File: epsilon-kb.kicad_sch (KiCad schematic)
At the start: 36 parts, among them J1 OLED-128x64, J2 OLED-128x32, J3 Conn_01x01, SW1 SW_Push, SW10 SW_Push, SW11 SW_SPDT, SW2 SW_Push, SW3 SW_Push, SW4 SW_Push, SW5 SW_Push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

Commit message: PCB
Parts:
- removed J3: Conn_01x01, symbol Connector_Generic:Conn_01x01
- added SW12: SW_Push, Button_Switch_THT:SW_PUSH_6mm, symbol Switch:SW_Push
- D1, D10, D2, D3, D4, D5, D6, D7, D8, D9: value SK6812MINI -> SK6812MINI-E; symbol LED:SK6812MINI -> sk6812mini-e:SK6812MINI-E
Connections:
- net +5V: now also D1.1 (VDD), D10.1 (VDD), D2.1 (VDD), D3.1 (VDD), D4.1 (VDD), D5.1 (VDD), D6.1 (VDD), D7.1 (VDD), D8.1 (VDD), D9.1 (VDD); no longer D1.4 (VDD), D10.4 (VDD), D2.4 (VDD), D3.4 (VDD), D4.4 (VDD), D5.4 (VDD), D6.4 (VDD), D7.4 (VDD), D8.4 (VDD), D9.4 (VDD)
- net GND: now also D1.3 (VSS), D10.3 (VSS), D2.3 (VSS), D3.3 (VSS), D4.3 (VSS), D5.3 (VSS), D6.3 (VSS), D7.3 (VSS), D8.3 (VSS), D9.3 (VSS), SW12.2; no longer D1.2 (VSS), D10.2 (VSS), D2.2 (VSS), D3.2 (VSS), D4.2 (VSS), D5.2 (VSS), D6.2 (VSS), D7.2 (VSS), D8.2 (VSS), D9.2 (VSS)
- net LED_IN: now also D1.4 (DIN); no longer D1.3 (DIN)
- net LED_OUT: now also D10.2 (DOUT); no longer D10.1 (DOUT)
- net RST: now reaches U1.17 (RESET)
- net RST: now also SW12.1
- new net: D2.2 (DOUT), D3.4 (DIN)
- new net: D1.2 (DOUT), D2.4 (DIN)
- new net: D10.4 (DIN), D9.2 (DOUT)
- new net: D8.2 (DOUT), D9.4 (DIN)
- new net: D6.2 (DOUT), D7.4 (DIN)
- new net: D5.2 (DOUT), D6.4 (DIN)
- new net: D7.2 (DOUT), D8.4 (DIN)
- new net: D4.2 (DOUT), D5.4 (DIN)
- new net: D3.2 (DOUT), D4.4 (DIN)

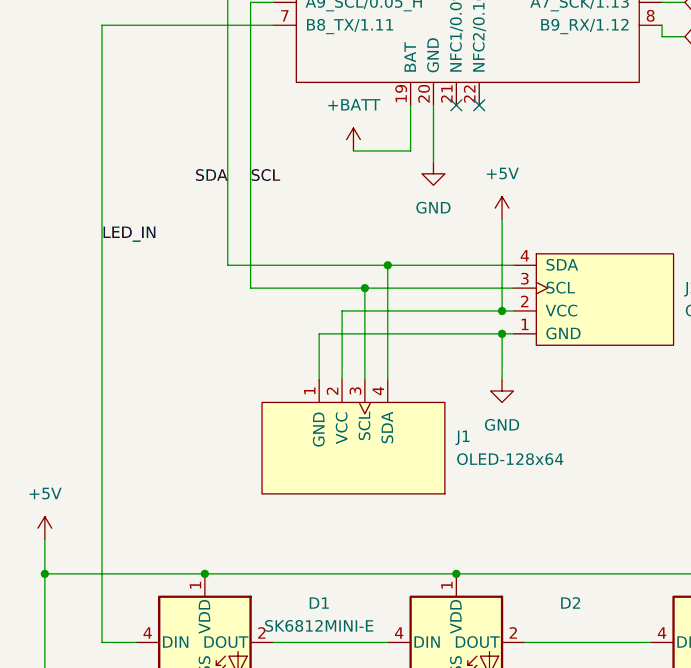
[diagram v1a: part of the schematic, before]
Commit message: add Makefile and images
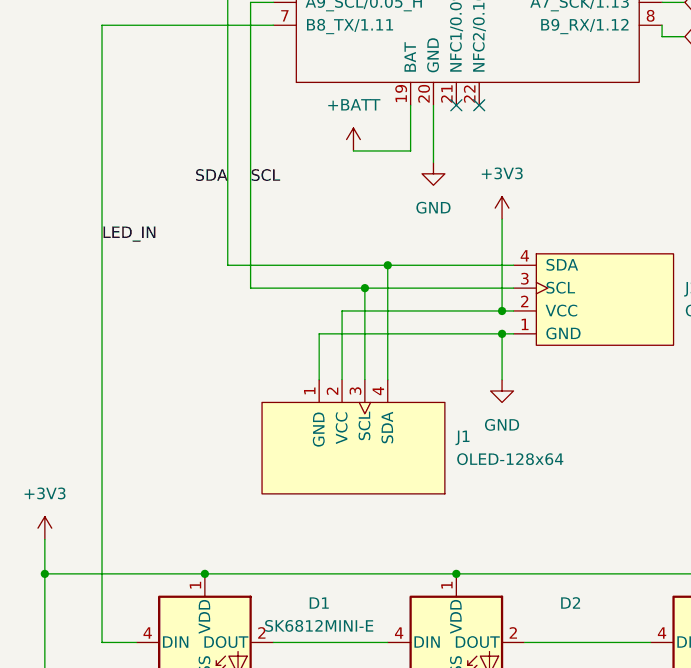
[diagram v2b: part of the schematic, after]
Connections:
- net +3V3: now also D1.1 (VDD), D10.1 (VDD), D2.1 (VDD), D3.1 (VDD), D4.1 (VDD), D5.1 (VDD), D6.1 (VDD), D7.1 (VDD), D8.1 (VDD), D9.1 (VDD), J1.2 (VCC), J2.2 (VCC)
- net +5V: no longer D1.1 (VDD), D10.1 (VDD), D2.1 (VDD), D3.1 (VDD), D4.1 (VDD), D5.1 (VDD), D6.1 (VDD), D7.1 (VDD), D8.1 (VDD), D9.1 (VDD), J1.2 (VCC), J2.2 (VCC)
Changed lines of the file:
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@@
     (pin "2")
-  )
-  (symbol (lib_id "power:+5V") (at 71.12 71.12 0) (unit 1)
-    (in_bom yes) (on_board yes) (fields_autoplaced)
-    (property "Reference" "#PWR0108" (id 0) (at 71.12 74.93 0)
-      (effects (font (size 1.27 1.27)) hide)
-    )
-    (property "Value" "+5V" (id 1) (at 71.12 66.04 0))
-    (property "Footprint" "" (id 2) (at 71.12 71.12 0)
-      (effects (font (size 1.27 1.27)) hide)
-    )
-    (property "Datasheet" "" (id 3) (at 71.12 71.12 0)
-      (effects (font (size 1.27 1.27)) hide)
-    )
-    (pin "1")
   )
   (symbol (lib_id "Diode:1N4148W") (at 156.21 33.02 270) (unit 1)
@@
     (pin "3")
   )
+  (symbol (lib_id "power:+3V3") (at 20.32 106.68 0) (unit 1)
+    (in_bom yes) (on_board yes) (fields_autoplaced)
+    (property "Reference" "#PWR?" (id 0) (at 20.32 110.49 0)
+      (effects (font (size 1.27 1.27)) hide)
+    )
+    (property "Value" "+3V3" (id 1) (at 20.32 101.6 0))
+    (property "Footprint" "" (id 2) (at 20.32 106.68 0)
+      (effects (font (size 1.27 1.27)) hide)
+    )
+    (property "Datasheet" "" (id 3) (at 20.32 106.68 0)
+      (effects (font (size 1.27 1.27)) hide)
+    )
+    (pin "1")
+  )
   (symbol (lib_id "power:GND") (at 233.68 48.26 0) (unit 1)
     (in_bom yes) (on_board yes) (fields_autoplaced)
@@
     (pin "2")
   )
+  (symbol (lib_id "power:+3V3") (at 71.12 71.12 0) (unit 1)
+    (in_bom yes) (on_board yes) (fields_autoplaced)
+    (property "Reference" "#PWR?" (id 0) (at 71.12 74.93 0)
+      (effects (font (size 1.27 1.27)) hide)
+    )
+    (property "Value" "+3V3" (id 1) (at 71.12 66.04 0))
+    (property "Footprint" "" (id 2) (at 71.12 71.12 0)
+      (effects (font (size 1.27 1.27)) hide)
+    )
+    (property "Datasheet" "" (id 3) (at 71.12 71.12 0)
+      (effects (font (size 1.27 1.27)) hide)
+    )
+    (pin "1")
+  )
   (symbol (lib_id "power:+BATT") (at 208.28 39.37 0) (unit 1)
     (in_bom yes) (on_board yes) (fields_autoplaced)
@@
     (pin "4")
   )
-  (symbol (lib_id "power:+5V") (at 20.32 106.68 0) (unit 1)
-    (in_bom yes) (on_board yes) (fields_autoplaced)
-    (property "Reference" "#PWR0112" (id 0) (at 20.32 110.49 0)
-      (effects (font (size 1.27 1.27)) hide)
-    )
-    (property "Value" "+5V" (id 1) (at 20.32 101.6 0))
-    (property "Footprint" "" (id 2) (at 20.32 106.68 0)
-      (effects (font (size 1.27 1.27)) hide)
-    )
-    (property "Datasheet" "" (id 3) (at 20.32 106.68 0)
-      (effects (font (size 1.27 1.27)) hide)
-    )
-    (pin "1")
-  )
   (symbol (lib_id "sk6812mini-e:SK6812MINI-E") (at 95.25 118.11 0) (unit 1)
     (in_bom yes) (on_board yes) (fields_autoplaced)
@@
       (reference "#PWR0107") (unit 1) (value "+3V3") (footprint "")
     )
-    (path "/24fca044-44d4-48b8-adbc-53d145353f3e"
-      (reference "#PWR0108") (unit 1) (value "+5V") (footprint "")
-    )
     (path "/6b34693b-ad0f-4557-b115-7499ecbd4196"
       (reference "#PWR0109") (unit 1) (value "GND") (footprint "")
@@
       (reference "#PWR0111") (unit 1) (value "GND") (footprint "")
     )
-    (path "/e017c7e0-b424-4c59-9ff0-5fbf749b6f64"
-      (reference "#PWR0112") (unit 1) (value "+5V") (footprint "")
+    (path "/8d62fc09-c1d1-4c28-817d-1951b4cff5d0"
+      (reference "#PWR?") (unit 1) (value "+3V3") (footprint "")
+    )
+    (path "/bffa5916-33be-4334-a7fb-b3d1011f8032"
+      (reference "#PWR?") (unit 1) (value "+3V3") (footprint "")
     )
     (path "/c2fb73c2-2f60-4a74-8d30-080a28406b0c"
